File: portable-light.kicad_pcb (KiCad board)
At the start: 2 copper layers, 96 parts, among them J1 Conn_01x08, J2 Prog, Q1 MMBT2222A, Q2 MMBT2222A, Q3 MMBT2222A, Q4 MMBT2222A, Q5 MMBT2222A, Q6 PHD45N03LTA, Q7 PHD45N03LTA, Q8 MMBT2222A, U1 ATmega88PA-AU, U2 L78L05_SOT89, U3 LTC1733EMSEPBF, X1 LOAD, Y1 Crystal

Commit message: Schematics and PCB layout complete
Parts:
- removed the C3 at (168.1, 108.1)
- removed the D2 at (152.1, 123.8)
- removed the R26 at (118.8, 102.0)
- added C1: 15n, Capacitor_SMD:C_1206_3216Metric_Pad1.42x1.75mm_HandSolder, F.Cu at (87.8, 51.7)
- added C5: 100n, Capacitor_SMD:C_1206_3216Metric_Pad1.42x1.75mm_HandSolder, F.Cu at (87.8, 54.3)
- added J3: Charger, Connector_PinHeader_2.54mm:PinHeader_1x02_P2.54mm_Vertical, F.Cu at (64.6, 81.5)
- added JP1: Jumper_2_Open, Jumper:SolderJumper-2_P1.3mm_Open_RoundedPad1.0x1.5mm, B.Cu at (76.8, 63.3)
- added NT1: Net-Tie_2, NetTie:NetTie-2_SMD_Pad0.5mm, B.Cu at (61.5, 63.6)
- added NT2: Net-Tie_2, NetTie:NetTie-2_SMD_Pad0.5mm, B.Cu at (84.9, 51.1)
- BT1: footprint Connector_PinHeader_1.00mm:PinHeader_1x02_P1.00mm_Vertical -> Connector_PinHeader_2.54mm:PinHeader_1x02_P2.54mm_Vertical
- C2: value 100n -> 15n
- C4: value 100n -> 330n
- R25: value 1MEG -> 500K
- moved D2 126.5 mm to (86.2, 57.5), turned to 180 degrees
- moved U2 116.7 mm to (100.2, 42.3), turned to 0 degrees
- moved D1 114.3 mm to (94.0, 58.9), turned to 80 degrees
- moved C25 113.2 mm to (99.8, 48.5), turned to 0 degrees
- moved R43 112.4 mm to (92.4, 52.2), turned to 180 degrees
- moved JP2 112.3 mm to (105.2, 49.6), turned to 90 degrees
- moved R41 110.4 mm to (93.0, 55.0), turned to 90 degrees
- moved R42 109.7 mm to (91.3, 55.1)
- moved D9 104.9 mm to (101.9, 53.5), turned to 0 degrees
- moved J4 100.5 mm to (68.8, 89.7), turned to 180 degrees
- moved D8 99.5 mm to (101.9, 57.2), turned to 180 degrees
- moved Q8 99.1 mm to (68.0, 40.1)
- moved R1 98.9 mm to (91.2, 41.3)
- moved R5 98.9 mm to (81.7, 41.2)
- moved R6 98.9 mm to (79.3, 41.2)
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- renumbered C9 to C10, C10 to C11, C11 to C12, C12 to C13, C13 to C14, C14 to C15, C15 to C16, C16 to C17, C17 to C20, C20 to C22, C22 to C23, C23 to C24, C24 to C25, C1 to C3, C5 to C6, C6 to C7, C7 to C8, C8 to C9, D3 to D2, D4 to D3, D5 to D4, D6 to D5, D7 to D6, D8 to D7, D9 to D8, D10 to D9, X1 to J4, JP1 to JP2, R27 to R26, R28 to R27, R29 to R28, R30 to R29, R31 to R30, R32 to R31, R33 to R32, R34 to R33, R35 to R34, R36 to R35, R37 to R36, R38 to R37, R39 to R38, R40 to R39, R41 to R40, R42 to R41, R43 to R42, R44 to R43
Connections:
- C15 pad 1: Net-(C14-Pad1) -> Net-(C15-Pad1)
- C2 pad 1: VBUS -> GNDA
- C2 pad 2: GNDPWR -> /sense_led
- C3 pad 2: GNDPWR -> GNDA
- C4 pad 2: GNDPWR -> GND
- C6 pad 1: GNDPWR -> GND
- C7 pad 1: GNDPWR -> GND
- D3 pad 2: Net-(C14-Pad1) -> Net-(C15-Pad1)
- J1 pad 8: GNDPWR -> GND
- J2 pad 1: GNDPWR -> GND
- J2 pad 5: /high_mos -> /mosi
- Q2 pad 3: Net-(D2-Pad2) -> Net-(C15-Pad1)
- Q8 pad 2: GNDPWR -> GND
- U1 pad 1: /low_mos -> /high_mos
- U1 pad 12: /pump-in -> /oc1a
- U1 pad 13: /oc1a -> /pump-in
- U1 pad 15: /high_mos -> /mosi
- U1 pad 21: GNDPWR -> GND
- U1 pad 3: GNDPWR -> GND
- U1 pad 31: /prog_pulldown -> /prog_pullup
- U1 pad 32: /prog_pullup -> /prog_pulldown
- U1 pad 5: GNDPWR -> GND
- U3 pad 8: VDC -> +BATT
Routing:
- net +15V: track 0.00 -> 71.4 mm
- net Net-(C18-Pad1): track 0.00 -> 67.2 mm, vias 0 -> 2
- net /high_mos: track 0.00 -> 66.0 mm, vias 0 -> 2
- net VBUS: track 0.00 -> 62.4 mm, vias 0 -> 1
- net /chrg_in: track 0.00 -> 61.6 mm, vias 0 -> 1
- net /low_mos: track 0.00 -> 51.4 mm, vias 0 -> 1
- net +BATT: track 0.00 -> 49.5 mm
- net Net-(R38-Pad1): track 0.00 -> 43.8 mm, vias 0 -> 2
- net Net-(R36-Pad1): track 0.00 -> 43.3 mm, vias 0 -> 2
- net /fault_in: track 0.00 -> 42.9 mm, vias 0 -> 2
- net /chrg_out: track 0.00 -> 33.4 mm, vias 0 -> 2
- net Net-(C15-Pad2): track 0.00 -> 30.9 mm
- net /oc1a: track 0.00 -> 25.7 mm
- net Net-(L1-Pad1): track 0.00 -> 22.4 mm
- net GNDPWR: track 0.00 -> 21.6 mm, vias 0 -> 10
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- added copper zone on B.Cu, net GND
- added copper zone on F.Cu, net GND
- added copper zone on B.Cu, net GNDA
- added copper zone on F.Cu, net GNDA
- added copper zone on B.Cu, net GNDPWR
- added copper zone on F.Cu, net GNDPWR
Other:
- board outline added: 50.5 x 63.7 mm
- copper layers 2 -> 4
- net class Default: via_dia 0.8 -> 1.8; via_drill 0.4 -> 1
- net class Thicc added: clearance 0.2, trace_width 0.5, via_dia 1.8, via_drill 1

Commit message: commit before checkout
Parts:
- moved BT1 1.52 mm to (62.5, 70.5)
- moved R25 0.22 mm to (60.6, 76.5), turned to 315 degrees
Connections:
- U3 pad 8: +BATT -> VDC
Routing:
- net VDC: track 16.0 -> 36.9 mm, vias 0 -> 1
- net +BATT: track 49.5 -> 56.9 mm
- net /fault_in: track 42.9 -> 46.4 mm
- net /chrg_out: track 33.4 -> 35.1 mm
- net /chrg_in: track 61.6 -> 63.0 mm

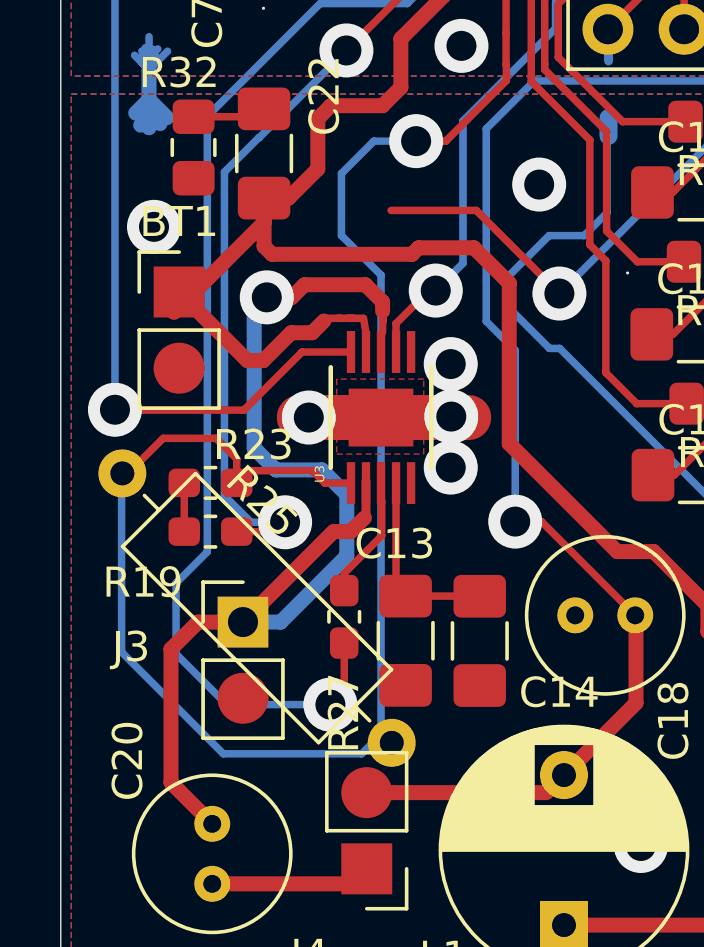
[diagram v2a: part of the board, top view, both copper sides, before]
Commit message: LTC1733 bug fixed
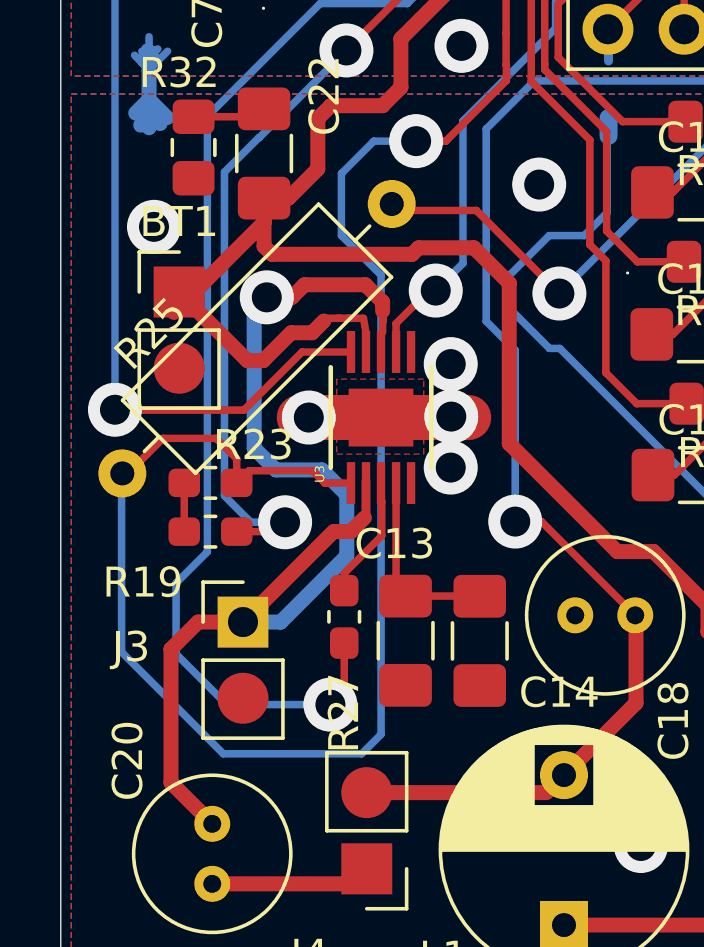
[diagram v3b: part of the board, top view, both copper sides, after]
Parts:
- turned R25 to 45 degrees

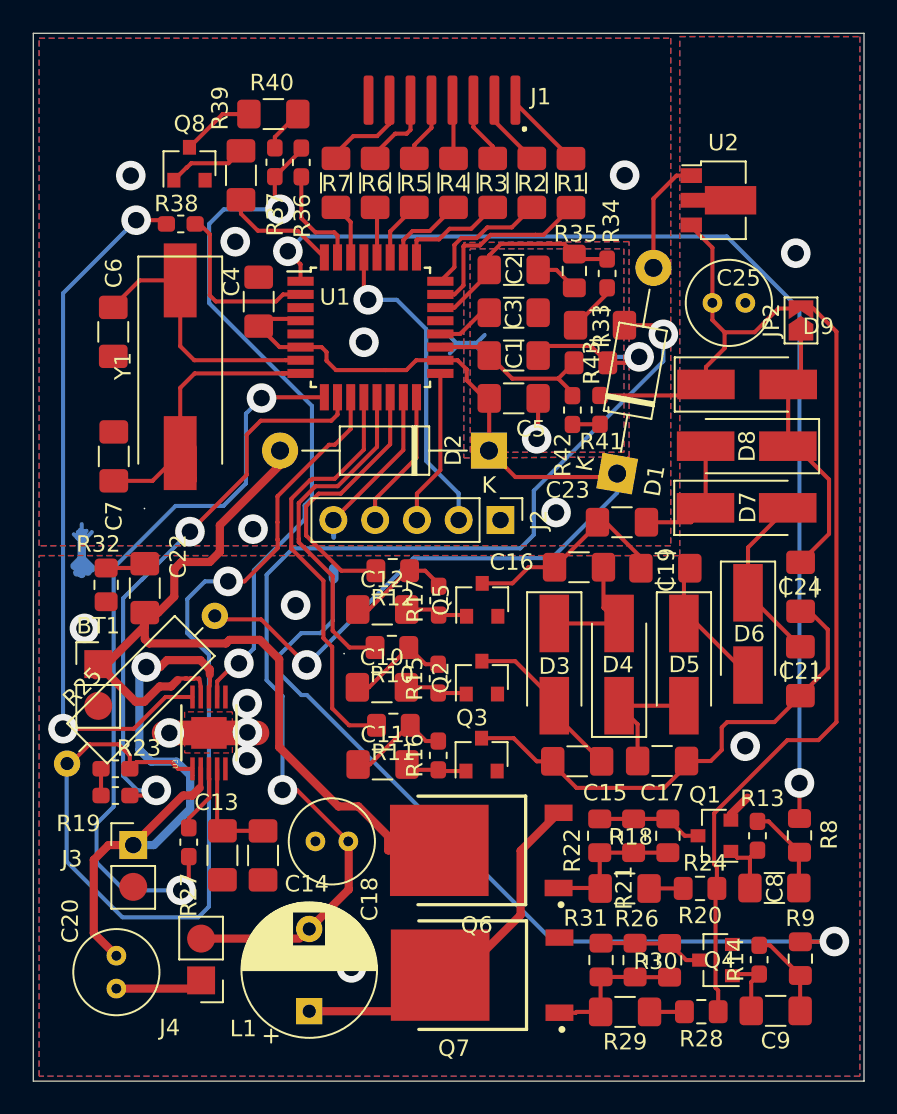
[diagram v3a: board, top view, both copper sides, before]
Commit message: AVR Charge-pump bug fixed
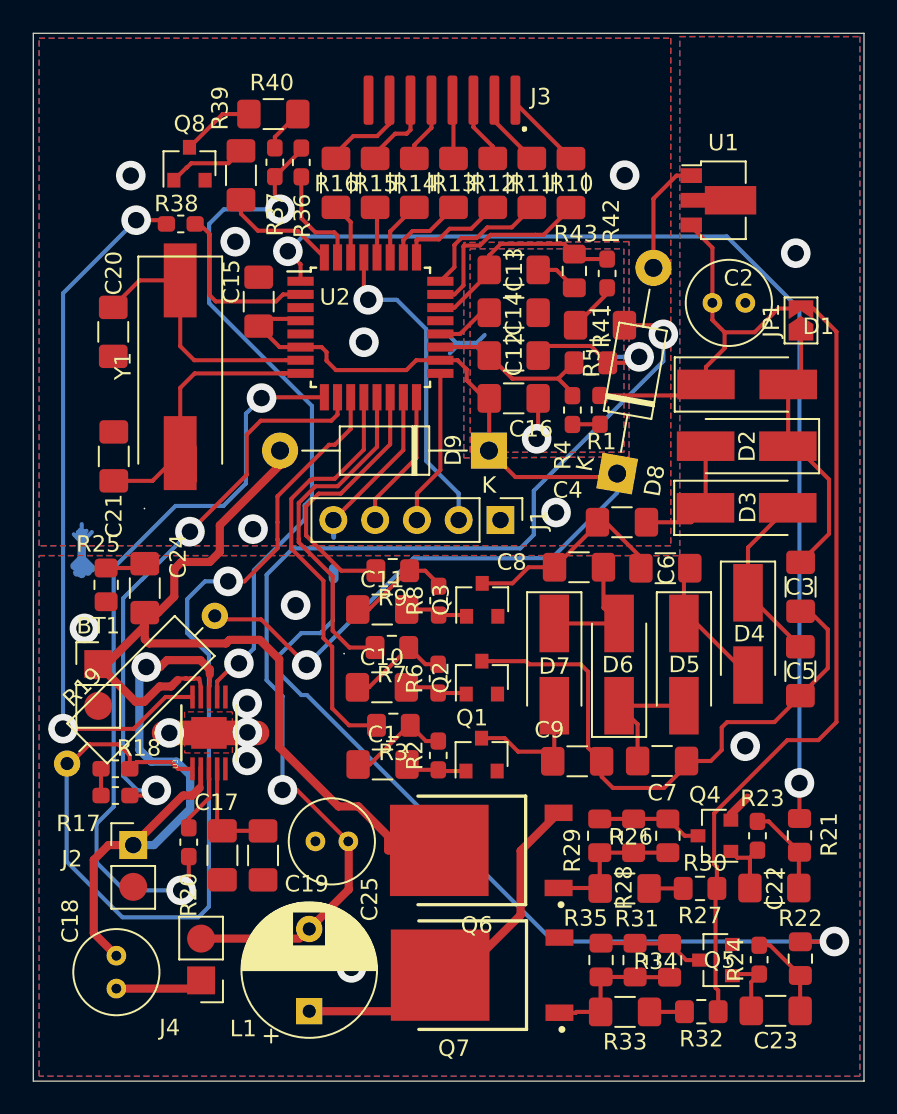
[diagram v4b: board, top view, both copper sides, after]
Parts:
- turned C9 to 0 degrees
- renumbered C11 to C1, C12 to C11, C1 to C12, C2 to C13, C3 to C14, C4 to C15, C5 to C16, C13 to C17, C20 to C18, C14 to C19, C25 to C2, C6 to C20, C7 to C21, C8 to C22, C9 to C23, C22 to C24, C18 to C25, C24 to C3, C23 to C4, C21 to C5, C19 to C6, C17 to C7, C16 to C8, C15 to C9, D9 to D1, D8 to D2, D7 to D3, D6 to D4, D4 to D6, D3 to D7, D1 to D8, D2 to D9, J2 to J1, J3 to J2, J1 to J3, JP2 to JP1, JP1 to JP2, Q3 to Q1, Q5 to Q3, Q1 to Q4, Q4 to Q5, R41 to R1, R1 to R10, R2 to R11, R3 to R12, R4 to R13, R5 to R14, R6 to R15, R7 to R16, R19 to R17, R23 to R18, R25 to R19, R16 to R2, R27 to R20, R8 to R21, R9 to R22, R13 to R23, R14 to R24, R32 to R25, R18 to R26, R20 to R27, R21 to R28, R22 to R29, R11 to R3, R24 to R30, R26 to R31, R28 to R32, R29 to R33, R30 to R34, R31 to R35, R42 to R4, R33 to R41, R34 to R42, R35 to R43, R43 to R5, R15 to R6, R10 to R7, R17 to R8, R12 to R9, U2 to U1, U1 to U2
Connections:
- net /high_mos renamed /high_mos_oc2a
- net /low_mos renamed /low_mos_oc2b
- net /oc1b renamed /pump-clkb_oc1b
- C3 pad 2: Net-(C15-Pad2) -> Net-(C3-Pad2)
- C5 pad 2: Net-(C15-Pad2) -> Net-(C3-Pad2)
- C7 pad 2: Net-(C15-Pad2) -> Net-(C3-Pad2)
- C9 pad 1: Net-(C15-Pad1) -> Net-(C9-Pad1)
- C9 pad 2: Net-(C15-Pad2) -> Net-(C3-Pad2)
- D7 pad 2: Net-(C15-Pad1) -> Net-(C9-Pad1)
- Q1 pad 3: Net-(C15-Pad2) -> Net-(C9-Pad1)
- Q2 pad 3: Net-(C15-Pad1) -> Net-(C3-Pad2)
- R3 pad 2: /oc1a -> /pump-in
- R7 pad 2: /pump-in -> /pump-clka_oc1a
- U2 pad 12: /oc1a -> /pump-in
- U2 pad 13: /pump-in -> /pump-clka_oc1a
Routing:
- net Net-(C3-Pad2): track 0.00 -> 35.9 mm
- net Net-(C15-Pad2): track 30.9 -> 0.00 mm
- net /oc1a: track 25.7 -> 0.00 mm
- net /pump-clka_oc1a: track 0.00 -> 20.8 mm
- net Net-(C15-Pad1): track 10.3 -> 0.00 mm
- net Net-(C9-Pad1): track 0.00 -> 9.33 mm
- net /pump-in: track 20.8 -> 25.7 mm

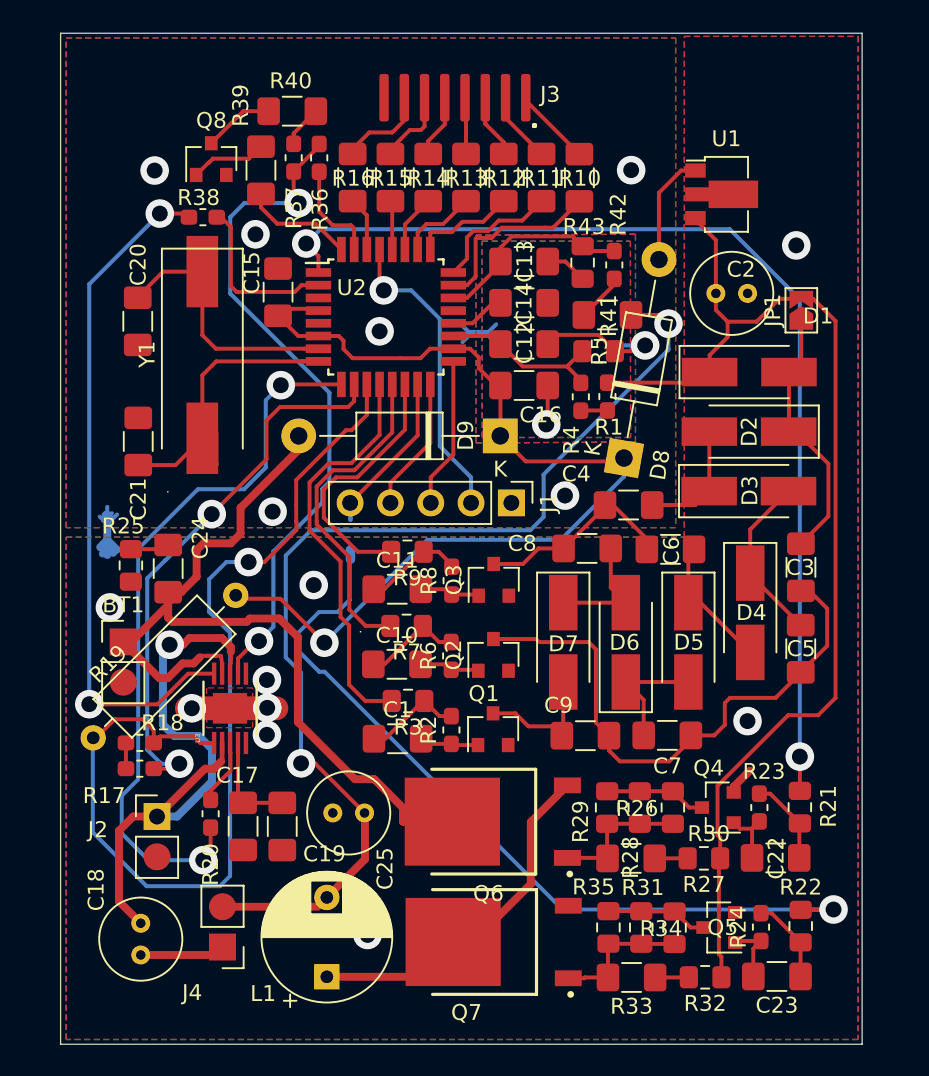
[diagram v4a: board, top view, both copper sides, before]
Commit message: Added push-button
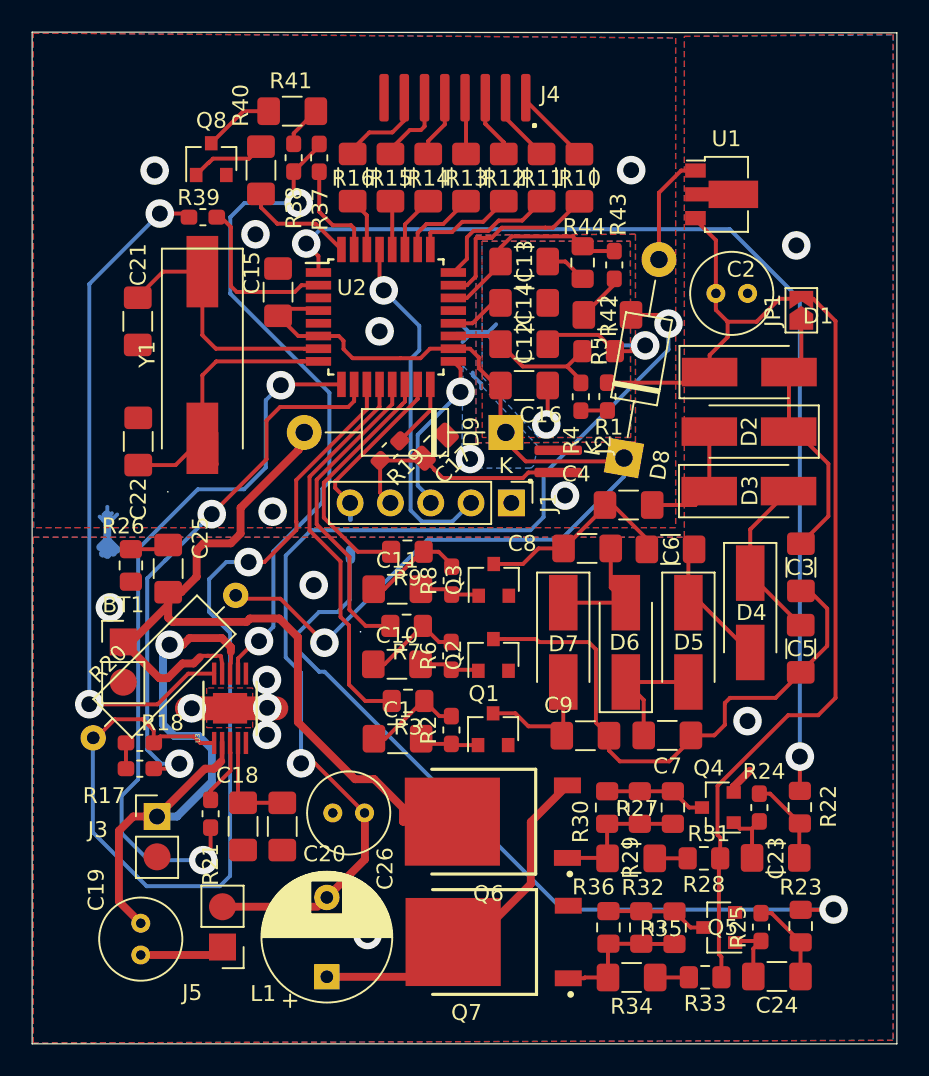
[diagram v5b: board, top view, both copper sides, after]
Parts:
- added C17: 300n, Capacitor_SMD:C_0805_2012Metric_Pad1.15x1.40mm_HandSolder, F.Cu at (82.1, 58.2)
- added J2: Button, Ribbon_Cable:Ribbon_2, F.Cu at (89.9, 59.8)
- added R19: 1K, Resistor_SMD:R_0603_1608Metric_Pad1.05x0.95mm_HandSolder, F.Cu at (79.3, 58.5)
- J4: renamed from J3; value Conn_01x08 -> Seven-segment
- moved D9 0.41 mm to (86.6, 57.3)
- renumbered C17 to C18, C18 to C19, C19 to C20, C20 to C21, C21 to C22, C22 to C23, C23 to C24, C24 to C25, C25 to C26, J2 to J3, J4 to J5, R19 to R20, R20 to R21, R21 to R22, R22 to R23, R23 to R24, R24 to R25, R25 to R26, R26 to R27, R27 to R28, R28 to R29, R29 to R30, R30 to R31, R31 to R32, R32 to R33, R33 to R34, R34 to R35, R35 to R36, R36 to R37, R37 to R38, R38 to R39, R39 to R40, R40 to R41, R41 to R42, R42 to R43, R43 to R44
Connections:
- J1 pad 4: /miso -> /miso-and-button
- U2 pad 16: /miso -> Net-(R19-Pad1)
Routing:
- net /miso-and-button: track 0.00 -> 14.9 mm
- net /miso: track 8.51 -> 0.00 mm
- net Net-(R19-Pad1): track 0.00 -> 4.35 mm
- net /reset: track 19.4 -> 22.3 mm
- net GND: track 17.5 -> 18.7 mm, vias 7 -> 8
- net /sck: track 9.50 -> 10.6 mm, vias 0 -> 1
- net /pump-in: track 25.7 -> 24.9 mm
- net /pump-clkb_oc1b: track 16.4 -> 15.6 mm
- net /pump-clka_oc1a: track 20.8 -> 20.0 mm
- net /mosi: track 10.2 -> 11.0 mm
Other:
- board size 50.5 x 63.7 mm -> 54.5 x 63.7 mm

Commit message: First review and refactoring complete; PCB is ready
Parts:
- removed the C15 at (72.2, 48.5)
- added C16: 300n, Capacitor_SMD:C_0805_2012Metric_Pad1.15x1.40mm_HandSolder, F.Cu at (137.9, 84.6)
- added C17: 100n, Capacitor_SMD:C_1206_3216Metric_Pad1.42x1.75mm_HandSolder, F.Cu at (163.1, 73.8)
- added C2: 100n, Capacitor_SMD:C_1206_3216Metric_Pad1.42x1.75mm_HandSolder, F.Cu at (167.3, 77.8)
- moved BT1 74.8 mm to (127.9, 106.7)
- moved C11 74.8 mm to (145.2, 108.1)
- moved C19 74.8 mm to (147.6, 94.4)
- moved C20 74.8 mm to (135.5, 118.3)
- moved C21 74.8 mm to (129.0, 124.4)
- moved C22 74.8 mm to (137.9, 118.3)
- moved C27 74.8 mm to (130.8, 102.1)
- moved C3 74.8 mm to (165.3, 84.7)
- moved C5 74.8 mm to (159.8, 98.0)
- moved C6 74.8 mm to (170.6, 107.1)
- moved C7 74.8 mm to (162.4, 100.8)
- moved C9 74.8 mm to (157.1, 100.8)
- moved D1 74.8 mm to (167.4, 89.7)
- moved D3 74.8 mm to (167.3, 97.2)
- moved D6 74.8 mm to (159.6, 106.7)
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- renumbered C9 to C10, C10 to C11, C11 to C12, C12 to C13, C13 to C14, C14 to C15, C16 to C18, C17 to C19, C18 to C20, C19 to C21, C20 to C22, C21 to C23, C22 to C24, C23 to C25, C24 to C26, C25 to C27, C26 to C28, C2 to C3, C3 to C4, C4 to C5, C5 to C6, C6 to C7, C7 to C8, C8 to C9
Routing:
- net +15V: track 71.4 -> 77.5 mm
- net Net-(C17-Pad1): track 7.09 -> 10.8 mm
- net Net-(C24-Pad2): track 18.7 -> 16.5 mm
- net GNDPWR: track 21.6 -> 23.8 mm, vias 10 -> 8
- net GND: track 18.7 -> 20.8 mm, vias 8 -> 10
- net Net-(R39-Pad1): track 43.8 -> 45.9 mm, vias 2 -> 0
- net Net-(R37-Pad1): track 43.3 -> 44.7 mm
